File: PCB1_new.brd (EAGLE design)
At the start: 101.4 x 47.5 mm, 71 parts

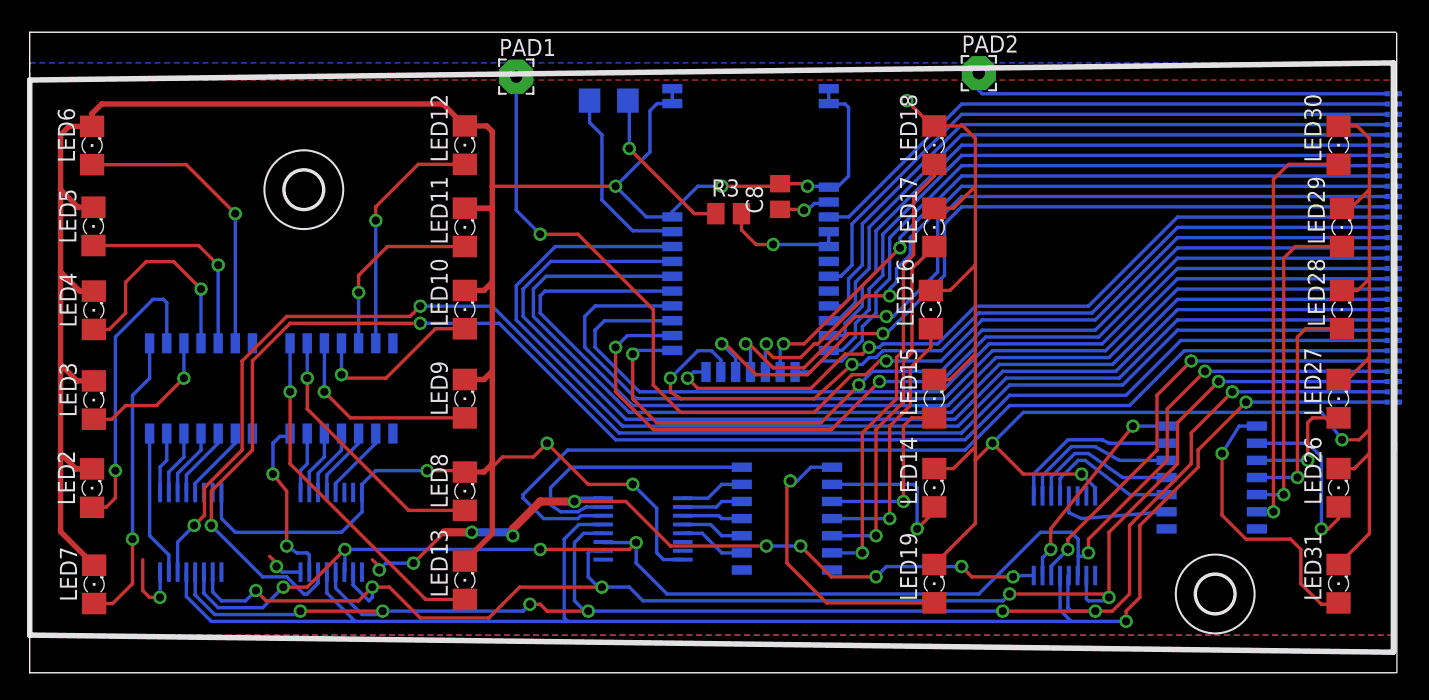
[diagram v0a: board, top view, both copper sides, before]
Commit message: Added ESD protection resistors on PCB1_new
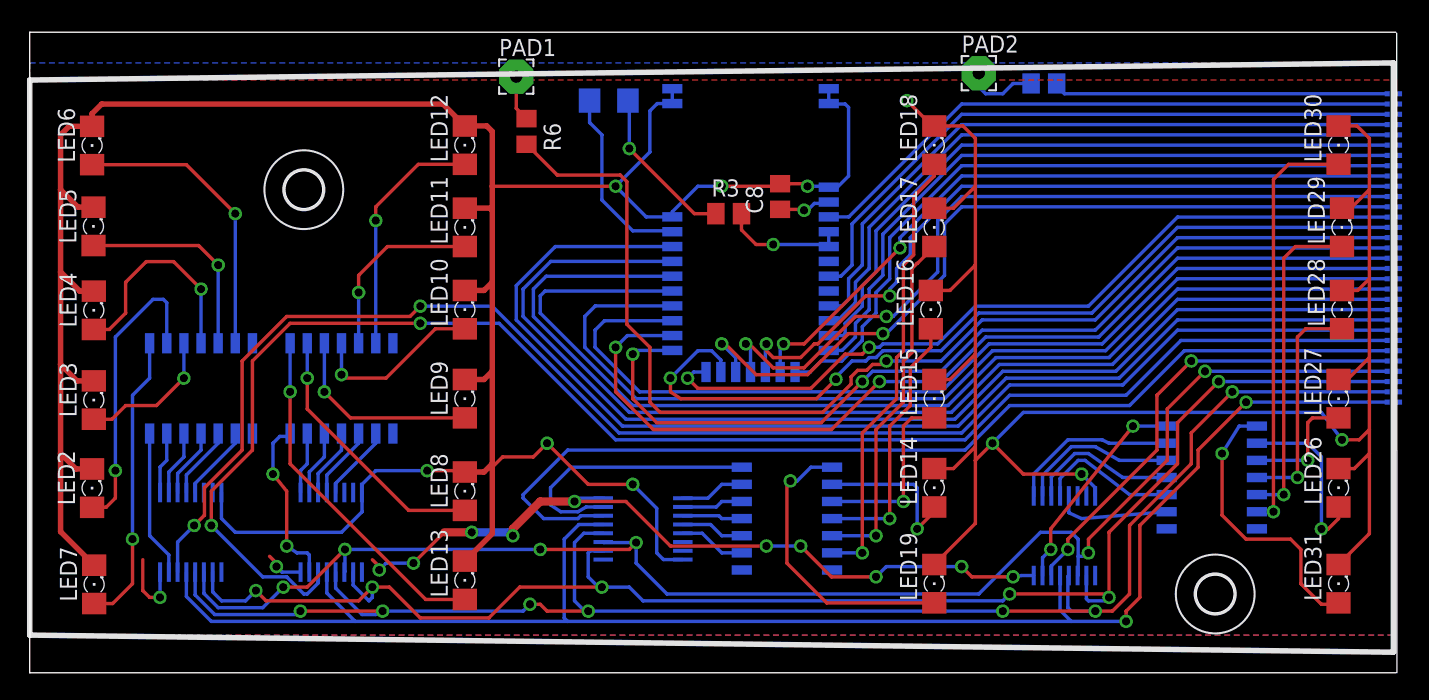
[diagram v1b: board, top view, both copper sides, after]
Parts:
- added R6, R7: 330k, rcl:R0805
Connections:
- new net N$116: PAD1.1, R6.1
- new net N$117: PAD2.1, R7.1
- net FRET1: now also R6.2; no longer PAD1.1
- net FRET2: now also R7.2; no longer PAD2.1
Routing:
- net FRET1: track 89.3 -> 45.4 mm, vias 2 -> 1
- net N$84: track 0.00 -> 40.9 mm
- net FRET2: track 31.6 -> 0.00 mm
- net N$52: track 0.00 -> 24.6 mm
- net N$117: track 0.00 -> 5.42 mm
- net N$116: track 0.00 -> 3.43 mm
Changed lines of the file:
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@@
 <element name="H1" library="holes" package="2,8" value="MOUNT-HOLE2.8" x="20.32" y="35.814"/>
 <element name="H2" library="holes" package="2,8" value="MOUNT-HOLE2.8" x="87.884" y="5.842"/>
+<element name="R6" library="rcl" package="R0805" value="330k" x="36.83" y="40.132" rot="R270"/>
+<element name="R7" library="rcl" package="R0805" value="330k" x="75.184" y="43.688" rot="MR180"/>
 </elements>
 <signals>
@@
 <wire x1="86.106" y1="23.114" x2="100.584" y2="23.114" width="0.254" layer="16"/>
 </signal>
-<signal name="FRET1">
-<contactref element="PAD1" pad="1"/>
-<wire x1="36.068" y1="44.196" x2="36.068" y2="34.29" width="0.254" layer="16"/>
-<wire x1="36.068" y1="34.29" x2="37.846" y2="32.512" width="0.254" layer="16"/>
-<via x="37.846" y="32.512" extent="1-16" drill="0.6"/>
-<wire x1="37.846" y1="32.512" x2="40.64" y2="32.512" width="0.254" layer="1"/>
-<wire x1="40.64" y1="32.512" x2="46.228" y2="26.924" width="0.254" layer="1"/>
-<wire x1="46.228" y1="26.924" x2="46.228" y2="21.336" width="0.254" layer="1"/>
-<wire x1="46.228" y1="21.336" x2="48.26" y2="19.304" width="0.254" layer="1"/>
-<wire x1="48.26" y1="19.304" x2="58.166" y2="19.304" width="0.254" layer="1"/>
-<wire x1="58.166" y1="19.304" x2="60.96" y2="22.098" width="0.254" layer="1"/>
-<wire x1="60.96" y1="22.098" x2="61.976" y2="22.098" width="0.254" layer="1"/>
-<wire x1="61.976" y1="22.098" x2="62.992" y2="23.114" width="0.254" layer="1"/>
-<wire x1="62.992" y1="23.114" x2="63.5" y2="23.114" width="0.254" layer="1"/>
-<via x="63.5" y="23.114" extent="1-16" drill="0.6"/>
-<wire x1="63.5" y1="23.114" x2="67.564" y2="23.114" width="0.254" layer="16"/>
-<wire x1="67.564" y1="23.114" x2="70.612" y2="26.162" width="0.254" layer="16"/>
-<wire x1="70.612" y1="26.162" x2="78.994" y2="26.162" width="0.254" layer="16"/>
-<wire x1="78.994" y1="26.162" x2="85.09" y2="32.258" width="0.254" layer="16"/>
-<wire x1="85.09" y1="32.258" x2="100.584" y2="32.258" width="0.254" layer="16"/>
-</signal>
-<signal name="FRET2">
-<contactref element="PAD2" pad="1"/>
-<wire x1="70.358" y1="44.45" x2="70.358" y2="43.18" width="0.254" layer="16"/>
-<wire x1="70.358" y1="43.18" x2="70.612" y2="42.926" width="0.254" layer="16"/>
-<wire x1="70.612" y1="42.926" x2="100.584" y2="42.926" width="0.254" layer="16"/>
-</signal>
 <signal name="WAKEUP">
 <contactref element="U$2" pad="P$7"/>
@@
 <wire x1="47.498" y1="21.844" x2="47.498" y2="20.828" width="0.254" layer="1"/>
 <wire x1="47.498" y1="20.828" x2="48.26" y2="20.32" width="0.254" layer="1"/>
-<wire x1="48.26" y1="20.32" x2="58.166" y2="20.32" width="0.254" layer="1"/>
-<wire x1="58.166" y1="20.32" x2="60.96" y2="22.86" width="0.254" layer="1"/>
-<via x="60.96" y="22.86" extent="1-16" drill="0.6"/>
 <wire x1="85.09" y1="33.02" x2="78.74" y2="26.67" width="0.254" layer="16"/>
 <wire x1="85.09" y1="33.02" x2="100.584" y2="33.02" width="0.254" layer="16"/>
-<wire x1="60.96" y1="22.86" x2="61.722" y2="22.86" width="0.254" layer="16"/>
-<wire x1="61.722" y1="22.86" x2="62.23" y2="23.368" width="0.254" layer="16"/>
+<wire x1="62.103" y1="23.241" x2="61.722" y2="22.86" width="0" layer="19" extent="1-16"/>
+<wire x1="62.103" y1="23.241" x2="62.23" y2="23.368" width="0" layer="19" extent="1-16"/>
 <wire x1="62.23" y1="23.368" x2="62.738" y2="23.368" width="0.254" layer="16"/>
 <wire x1="63.246" y1="23.876" x2="62.738" y2="23.368" width="0.254" layer="16"/>
@@
 <wire x1="78.74" y1="26.67" x2="70.358" y2="26.67" width="0.254" layer="16"/>
 <wire x1="67.564" y1="23.876" x2="63.246" y2="23.876" width="0.254" layer="16"/>
+<wire x1="58.32860625" y1="20.32" x2="59.771303125" y2="21.762696875" width="0.254" layer="1"/>
+<via x="59.771303125" y="21.762696875" extent="1-16" drill="0.6"/>
+<wire x1="59.771303125" y1="21.762696875" x2="59.771303125" y2="21.925303125" width="0.254" layer="16"/>
+<wire x1="60.96" y1="23.114" x2="61.976" y2="23.114" width="0.254" layer="16"/>
+<wire x1="61.976" y1="23.114" x2="62.23" y2="23.368" width="0.254" layer="16"/>
+<wire x1="48.26" y1="20.32" x2="58.32860625" y2="20.32" width="0.254" layer="1"/>
+<wire x1="59.771303125" y1="21.925303125" x2="60.96" y2="23.114" width="0.254" layer="16"/>
 </signal>
 <signal name="RST_N">
@@
 <wire x1="44.704" y1="20.32" x2="46.482" y2="18.542" width="0.254" layer="1"/>
 <wire x1="46.482" y1="18.542" x2="58.674" y2="18.542" width="0.254" layer="1"/>
-<wire x1="58.674" y1="18.542" x2="61.468" y2="21.336" width="0.254" layer="1"/>
-<via x="61.468" y="21.336" extent="1-16" drill="0.6"/>
-<wire x1="61.468" y1="21.336" x2="62.484" y2="22.352" width="0.254" layer="16"/>
+<wire x1="58.674" y1="18.542" x2="61.722" y2="21.59" width="0.254" layer="1"/>
+<via x="61.722" y="21.59" extent="1-16" drill="0.6"/>
+<wire x1="61.722" y1="21.59" x2="62.484" y2="22.352" width="0.254" layer="16"/>
 <wire x1="62.484" y1="22.352" x2="67.564" y2="22.352" width="0.254" layer="16"/>
 <wire x1="67.564" y1="22.352" x2="70.612" y2="25.4" width="0.254" layer="16"/>
@@
 <signal name="N$52">
 <contactref element="U$6" pad="P$2"/>
+<wire x1="100.638" y1="42.926" x2="76.708" y2="42.926" width="0.254" layer="16"/>
+<wire x1="76.708" y1="42.926" x2="76.2" y2="43.434" width="0.254" layer="16"/>
 </signal>
 <signal name="N$53">
@@
 <signal name="N$84">
 <contactref element="U$20" pad="P$2"/>
+<wire x1="100.638" y1="32.258" x2="85.09" y2="32.258" width="0.254" layer="16"/>
+<wire x1="85.09" y1="32.258" x2="78.994" y2="26.162" width="0.254" layer="16"/>
+<wire x1="78.994" y1="26.162" x2="70.612" y2="26.162" width="0.254" layer="16"/>
+<wire x1="70.612" y1="26.162" x2="67.564" y2="23.114" width="0.254" layer="16"/>
+<wire x1="67.564" y1="23.114" x2="63.5" y2="23.114" width="0.254" layer="16"/>
+<wire x1="63.5" y1="23.114" x2="63.5" y2="23.114" width="0" layer="19" extent="1-16"/>
 </signal>
 <signal name="N$85">
@@
 <contactref element="U$9" pad="P$1"/>
 </signal>
+<signal name="N$116">
+<contactref element="PAD1" pad="1"/>
+<contactref element="R6" pad="1"/>
+<wire x1="36.068" y1="44.196" x2="36.068" y2="41.844" width="0.254" layer="1"/>
+<wire x1="36.068" y1="41.844" x2="36.83" y2="41.082" width="0.254" layer="1"/>
+</signal>
+<signal name="N$117">
+<contactref element="PAD2" pad="1"/>
+<contactref element="R7" pad="1"/>
+<wire x1="74.234" y1="43.688" x2="72.898" y2="43.688" width="0.254" layer="16"/>
+<wire x1="72.898" y1="43.688" x2="72.136" y2="42.926" width="0.254" layer="16"/>
+<wire x1="72.136" y1="42.926" x2="70.866" y2="42.926" width="0.254" layer="16"/>
+<wire x1="70.866" y1="42.926" x2="70.358" y2="43.434" width="0.254" layer="16"/>
+<wire x1="70.358" y1="43.434" x2="70.358" y2="44.45" width="0.254" layer="16"/>
+</signal>
+<signal name="FRET2">
+<contactref element="R7" pad="2"/>
+</signal>
+<signal name="FRET1">
+<contactref element="R6" pad="2"/>
+<wire x1="43.77920625" y1="36.9014" x2="44.2674" y2="36.41320625" width="0.254" layer="1"/>
+<wire x1="36.83" y1="39.182" x2="39.1106" y2="36.9014" width="0.254" layer="1"/>
+<wire x1="39.1106" y1="36.9014" x2="43.77920625" y2="36.9014" width="0.254" layer="1"/>
+<wire x1="44.2674" y1="36.41320625" x2="44.2674" y2="25.8366" width="0.254" layer="1"/>
+<wire x1="44.2674" y1="25.8366" x2="45.974" y2="24.13" width="0.254" layer="1"/>
+<wire x1="45.974" y1="24.13" x2="45.974" y2="20.066" width="0.254" layer="1"/>
+<wire x1="45.974" y1="20.066" x2="46.736" y2="19.304" width="0.254" layer="1"/>
+<wire x1="46.736" y1="19.304" x2="58.78941875" y2="19.304" width="0.254" layer="1"/>
+<wire x1="58.78941875" y1="19.304" x2="60.8886" y2="21.40318125" width="0.254" layer="1"/>
+<wire x1="60.8886" y1="21.40318125" x2="60.8886" y2="21.93520625" width="0.254" layer="1"/>
+<wire x1="60.8886" y1="21.93520625" x2="61.37679375" y2="22.4234" width="0.254" layer="1"/>
+<wire x1="61.37679375" y1="22.4234" x2="62.0474" y2="22.4234" width="0.254" layer="1"/>
+<wire x1="62.0474" y1="22.4234" x2="62.484" y2="22.86" width="0.254" layer="1"/>
+<wire x1="63.246" y1="22.86" x2="63.5" y2="23.114" width="0.254" layer="1"/>
+<via x="63.5" y="23.114" extent="1-16" drill="0.6"/>
+<wire x1="62.484" y1="22.86" x2="63.246" y2="22.86" width="0.254" layer="1"/>
+</signal>
 </signals>

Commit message: Finished changing dimensions for PCB3 and switched out resistors for smaller ones.
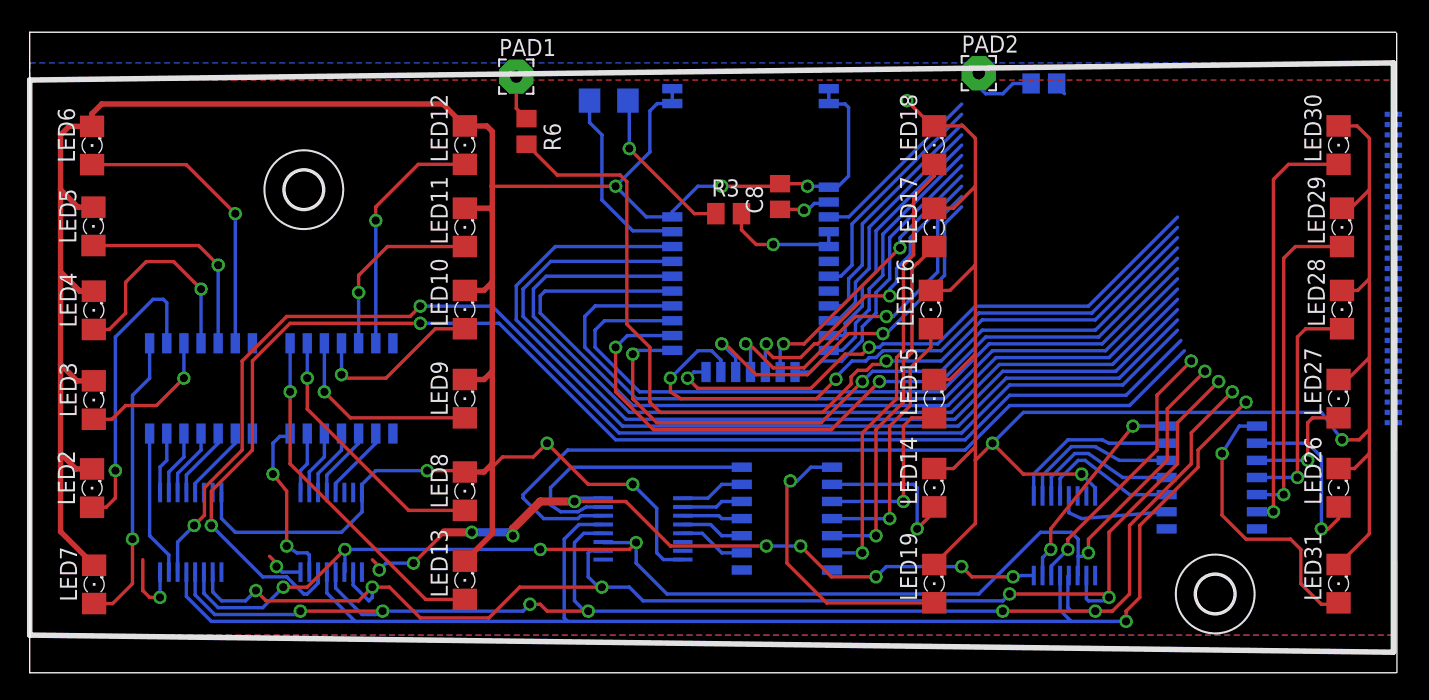
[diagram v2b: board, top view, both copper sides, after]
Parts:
- moved U$35 20.6 mm to (101.1, 41.4)
- moved U$34 19.1 mm to (101.1, 40.6)
- moved U$33 17.5 mm to (101.1, 39.9)
- moved U$30 6.10 mm to (101.1, 18.5)
- moved U$31 4.57 mm to (101.1, 19.3)
- moved U$10 3.81 mm to (101.1, 36.1)
- moved U$11 3.81 mm to (101.1, 35.3)
- moved U$12 3.81 mm to (101.1, 34.5)
- moved U$13 3.81 mm to (101.1, 33.8)
- moved U$19 3.81 mm to (101.1, 29.2)
- moved U$20 3.81 mm to (101.1, 28.4)
- moved U$22 3.81 mm to (101.1, 26.9)
- moved U$23 3.81 mm to (101.1, 26.2)
- moved U$24 3.81 mm to (101.1, 25.4)
- moved U$6 3.81 mm to (101.1, 39.1)
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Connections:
- removed net N$100: U$31.P$1
- removed net N$101: U$30.P$1
- removed net N$102: U$29.P$1
- removed net N$103: U$28.P$1
- removed net N$104: U$27.P$1
- removed net N$105: U$26.P$1
- removed net N$106: U$25.P$1
- removed net N$107: U$24.P$1
- removed net N$108: U$23.P$1
- removed net N$109: U$22.P$1
- removed net N$110: U$21.P$1
- removed net N$111: U$20.P$1
- removed net N$112: U$19.P$1
- removed net N$113: U$18.P$1
- removed net N$114: U$17.P$1
- removed net N$115: U$16.P$1
- removed net N$13: U$35.P$1
- removed net N$14: U$1.10, U$3.10, U$4.10, U$5.10
- removed net N$17: U$35.P$2
- removed net N$18: U$34.P$1
- removed net N$31: U$34.P$2
- removed net N$32: U$33.P$2
- removed net N$33: U$33.P$1
- removed net N$34: U$6.P$1
- removed net N$42: U$7.P$1
- removed net N$45: U$8.P$1
- removed net N$48: U$1.11, U$3.11, U$4.11, U$5.11
- removed net N$50: U$9.P$1
- removed net N$51: U$1.12, U$3.12, U$4.12, U$5.12
- removed net N$52: U$6.P$2
- removed net N$53: U$7.P$2
- removed net N$54: U$8.P$2
- removed net N$55: U$9.P$2
- removed net N$56: U$10.P$1
- removed net N$57: U$11.P$1
- removed net N$58: U$10.P$2
- removed net N$59: U$11.P$2
- removed net N$65: U$12.P$2
- removed net N$73: U$12.P$1
- removed net N$74: U$13.P$1
- removed net N$75: U$13.P$2
- removed net N$76: U$14.P$2
- removed net N$77: U$14.P$1
- removed net N$78: U$15.P$1
- removed net N$79: U$15.P$2
- removed net N$80: U$16.P$2
- removed net N$81: U$17.P$2
- removed net N$82: U$18.P$2
- removed net N$83: U$19.P$2
- removed net N$84: U$20.P$2
- removed net N$85: U$21.P$2
- removed net N$86: U$22.P$2
- removed net N$87: U$23.P$2
- removed net N$88: U$24.P$2
- removed net N$89: U$25.P$2
- removed net N$90: U$26.P$2
- removed net N$91: U$27.P$2
- removed net N$92: U$28.P$2
- removed net N$93: U$29.P$2
- removed net N$94: U$30.P$2
- removed net N$95: U$31.P$2
- removed net N$96: U$32.P$2
- removed net N$97: U$36.P$2
- removed net N$98: U$36.P$1
- removed net N$99: U$32.P$1
- new net RCK: U$1.12, U$3.12, U$31.P$1, U$31.P$2, U$4.12, U$5.12
- new net SCK: U$1.11, U$3.11, U$32.P$1, U$32.P$2, U$4.11, U$5.11
- new net SCLR: U$1.10, U$3.10, U$36.P$1, U$36.P$2, U$4.10, U$5.10
- net EAN: now also U$26.P$1, U$26.P$2
- net FRET1: now also U$19.P$1, U$19.P$2
- net FRET2: now also U$20.P$1, U$20.P$2
- net G: now also U$30.P$1, U$30.P$2
- net LED_SER1: now also U$15.P$1, U$15.P$2
- net LED_SER2: now also U$16.P$1, U$16.P$2
- net LED_SER3: now also U$17.P$1, U$17.P$2
- net LED_SER4: now also U$18.P$1, U$18.P$2
- net P0_0: now also U$23.P$1, U$23.P$2
- net P0_4: now also U$13.P$1, U$13.P$2
- net P0_5: now also U$22.P$1, U$22.P$2
- net P1_2: now also U$29.P$1, U$29.P$2
- net P1_3: now also U$28.P$1, U$28.P$2
- net P1_5: now also U$14.P$1, U$14.P$2
- net P1_7: now also U$21.P$1, U$21.P$2
- net P2_0: now also U$24.P$1, U$24.P$2
- net P2_4: now also U$25.P$1, U$25.P$2
- net P3_1: now also U$33.P$1, U$33.P$2
- net P3_2: now also U$6.P$1, U$6.P$2
- net P3_3: now also U$7.P$1, U$7.P$2
- net P3_4: now also U$8.P$1, U$8.P$2
- net P3_6: now also U$9.P$1, U$9.P$2
- net P3_7: now also U$10.P$1, U$10.P$2
- net RST_N: now also U$27.P$1, U$27.P$2
- net RXD: now also U$35.P$1, U$35.P$2
- net SW_BTN: now also U$12.P$1, U$12.P$2
- net TXD: now also U$34.P$1, U$34.P$2
- net WAKEUP: now also U$11.P$1, U$11.P$2
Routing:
- net N$51: track 120.4 -> 0.00 mm, vias 7 -> 0
- net N$14: track 115.3 -> 0.00 mm, vias 6 -> 0
- net N$48: track 111.7 -> 0.00 mm, vias 6 -> 0
- net RCK: track 0.00 -> 109.0 mm, vias 0 -> 7
- net SCLR: track 0.00 -> 102.8 mm, vias 0 -> 6
- net SCK: track 0.00 -> 98.2 mm, vias 0 -> 6
- net N$84: track 40.9 -> 0.00 mm
- net P1_3: track 50.6 -> 19.1 mm
- net P0_4: track 49.6 -> 18.1 mm
- net WAKEUP: track 48.1 -> 16.6 mm
- net SW_BTN: track 44.8 -> 13.3 mm
- net P2_4: track 60.1 -> 28.6 mm
- net P2_0: track 58.0 -> 26.5 mm
- net P1_7: track 53.5 -> 22.0 mm
- net P1_5: track 49.7 -> 18.2 mm
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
